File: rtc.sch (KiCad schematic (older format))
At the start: 8 parts, among them U3 RV-4162-C7

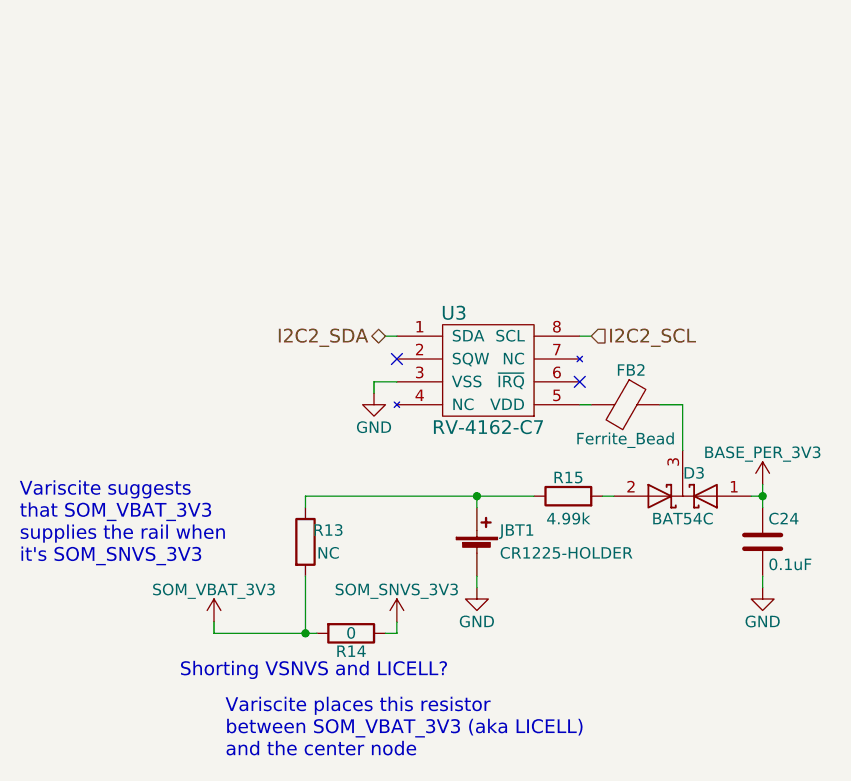
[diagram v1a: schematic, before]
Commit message: Add the board ID EEPROM chip and move the 0Ohm resistor such that the coin cell battery would actually power SOM_SNVS_3V3 when removed and the NC resistor is populated
This re-arrengment of the resistor makes the reference schematic more clear knowing that SOM_VBAT_3V3 is not actually LICELL.
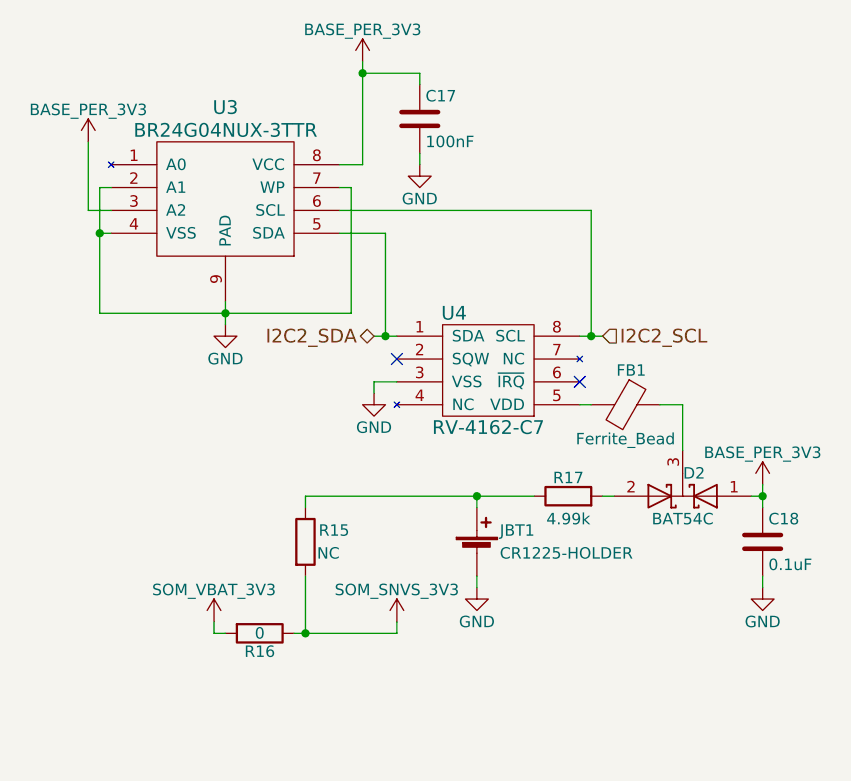
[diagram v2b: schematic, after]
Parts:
- added C17: 100nF, symbol C
- added U3: BR24G04NUX-3TTR, symbol BR24G04NUX-3TTR
- renumbered C24 to C18, D3 to D2, FB2 to FB1, R13 to R15, R14 to R16, R15 to R17, U3 to U4
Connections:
- net BASE_PER_3V3: now also C17.1, U3.3 (A2), U3.8 (VCC)
- net GND: now also C17.2, U3.2 (A1), U3.4 (VSS), U3.7 (WP), U3.9 (PAD)
- net I2C2_SCL: now also U3.6 (SCL)
- net I2C2_SDA: now also U3.5 (SDA)
- net SOM_SNVS_3V3: now also R15.2
- net SOM_VBAT_3V3: no longer R15.2
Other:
- note removed: "Shorting VSNVS and LICELL?"
- note removed: "Variscite places this resistor\nbetween SOM_VBAT_3V3 (aka LICELL)\nand the center node"
- note removed: "Variscite suggests\nthat SOM_VBAT_3V3\nsupplies the rail when\nit's SOM_SNVS_3V3"
- moved on the sheet: R16
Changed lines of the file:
@@
 $EndDescr
 $Comp
-L SOM_SNVS_3V3 #PWR041
+L SOM_SNVS_3V3 #PWR040
 U 1 1 5AC54E36
 P 5100 4300
-F 0 "#PWR041" H 5100 4150 50  0001 C CNN
+F 0 "#PWR040" H 5100 4150 50  0001 C CNN
 F 1 "SOM_SNVS_3V3" H 5100 4440 50  0000 C CNN
 F 2 "" H 5100 4300 50  0001 C CNN
@@
 $EndComp
 $Comp
-L R R14
+L R R16
 U 1 1 5AC54E4A
-P 4900 4350
-F 0 "R14" V 4980 4350 50  0000 C CNN
-F 1 "0" V 4900 4350 50  0000 C CNN
-F 2 "" V 4830 4350 50  0001 C CNN
-F 3 "" H 4900 4350 50  0001 C CNN
-	1    4900 4350
+P 4500 4350
+F 0 "R16" V 4580 4350 50  0000 C CNN
+F 1 "0" V 4500 4350 50  0000 C CNN
+F 2 "" V 4430 4350 50  0001 C CNN
+F 3 "" H 4500 4350 50  0001 C CNN
+	1    4500 4350
 	0    1    1    0
 $EndComp
 $Comp
-L SOM_VBAT_3V3 #PWR042
+L SOM_VBAT_3V3 #PWR041
 U 1 1 5AC54E9B
 P 4300 4300
-F 0 "#PWR042" H 4300 4150 50  0001 C CNN
+F 0 "#PWR041" H 4300 4150 50  0001 C CNN
 F 1 "SOM_VBAT_3V3" H 4300 4440 50  0000 C CNN
 F 2 "" H 4300 4300 50  0001 C CNN
@@
 	4300 4300 4300 4350
 $Comp
-L R R13
+L R R15
 U 1 1 5AC553FE
 P 4700 3950
-F 0 "R13" H 4800 4000 50  0000 C CNN
+F 0 "R15" H 4825 4000 50  0000 C CNN
 F 1 "NC" H 4800 3900 50  0000 C CNN
 F 2 "" V 4630 3950 50  0001 C CNN
@@
 $EndComp
 $Comp
-L D_Schottky_x2_KCom_AAK D3
+L D_Schottky_x2_KCom_AAK D2
 U 1 1 5AC55F7F
 P 6350 3750
-F 0 "D3" H 6300 3650 50  0000 C CNN
+F 0 "D2" H 6300 3650 50  0000 C CNN
 F 1 "BAT54C" H 6350 3850 50  0000 C CNN
 F 2 "" H 6350 3750 50  0001 C CNN
@@
 $EndComp
 $Comp
-L BASE_PER_3V3 #PWR043
+L BASE_PER_3V3 #PWR042
 U 1 1 5AC5AC58
 P 6700 3700
-F 0 "#PWR043" H 6700 3550 50  0001 C CNN
+F 0 "#PWR042" H 6700 3550 50  0001 C CNN
 F 1 "BASE_PER_3V3" H 6700 3840 50  0000 C CNN
 F 2 "" H 6700 3700 50  0001 C CNN
@@
 	6700 3700 6700 3800
 $Comp
-L R R15
+L R R17
 U 1 1 5AC5AF1B
 P 5850 3750
-F 0 "R15" V 5930 3750 50  0000 C CNN
+F 0 "R17" V 5930 3750 50  0000 C CNN
 F 1 "4.99k" V 5750 3750 50  0000 C CNN
 F 2 "" V 5780 3750 50  0001 C CNN
@@
 $EndComp
 $Comp
-L Ferrite_Bead FB2
+L Ferrite_Bead FB1
 U 1 1 5AC5AF7B
 P 6100 3350
-F 0 "FB2" V 5950 3375 50  0000 C CNN
+F 0 "FB1" V 5950 3375 50  0000 C CNN
 F 1 "Ferrite_Bead" V 6250 3350 50  0000 C CNN
 F 2 "" V 6030 3350 50  0001 C CNN
@@
 	6050 3750 6000 3750
 $Comp
-L C C24
+L C C18
 U 1 1 5AC5B61C
 P 6700 3950
-F 0 "C24" H 6725 4050 50  0000 L CNN
+F 0 "C18" H 6725 4050 50  0000 L CNN
 F 1 "0.1uF" H 6725 3850 50  0000 L CNN
 F 2 "" H 6738 3800 50  0001 C CNN
@@
 $EndComp
 $Comp
-L GND #PWR044
+L GND #PWR043
 U 1 1 5AC5B669
 P 6700 4150
-F 0 "#PWR044" H 6700 3900 50  0001 C CNN
+F 0 "#PWR043" H 6700 3900 50  0001 C CNN
 F 1 "GND" H 6700 4000 50  0000 C CNN
 F 2 "" H 6700 4150 50  0001 C CNN
@@
 Connection ~ 6700 3750
 $Comp
-L RV-4162-C7 U3
+L RV-4162-C7 U4
 U 1 1 5AC5BD52
 P 5500 3200
-F 0 "U3" H 5350 3450 60  0000 C CNN
+F 0 "U4" H 5350 3450 60  0000 C CNN
 F 1 "RV-4162-C7" H 5500 2950 60  0000 C CNN
 F 2 "" H 5600 2950 60  0001 C CNN
@@
 	4700 3750 5700 3750
 $Comp
-L GND #PWR045
+L GND #PWR044
 U 1 1 5AC5D6B6
 P 5450 4150
-F 0 "#PWR045" H 5450 3900 50  0001 C CNN
+F 0 "#PWR044" H 5450 3900 50  0001 C CNN
 F 1 "GND" H 5450 4000 50  0000 C CNN
 F 2 "" H 5450 4150 50  0001 C CNN
@@
 	4700 3800 4700 3750
 Connection ~ 5450 3750
-Text Notes 4350 4900 0    60   ~ 0
-Variscite places this resistor\nbetween SOM_VBAT_3V3 (aka LICELL)\nand the center node
-Text Notes 3450 4050 0    60   ~ 0
-Variscite suggests\nthat SOM_VBAT_3V3\nsupplies the rail when\nit's SOM_SNVS_3V3
-Wire Wire Line
-	5050 4350 5100 4350
-Wire Wire Line
-	4300 4350 4750 4350
-Text Notes 4150 4550 0    60   ~ 0
-Shorting VSNVS and LICELL?
-Text HLabel 5050 3050 0    60   BiDi ~ 0
+Text HLabel 5000 3050 0    60   BiDi ~ 0
 I2C2_SDA
-Text HLabel 5950 3050 2    60   Input ~ 0
+Text HLabel 6000 3050 2    60   Input ~ 0
 I2C2_SCL
 Wire Wire Line
-	5050 3050 5100 3050
-Wire Wire Line
-	5950 3050 5900 3050
-$Comp
-L GND #PWR046
+	5000 3050 5100 3050
+Wire Wire Line
+	5900 3050 6000 3050
+$Comp
+L GND #PWR045
 U 1 1 5AC6302E
 P 5000 3300
-F 0 "#PWR046" H 5000 3050 50  0001 C CNN
+F 0 "#PWR045" H 5000 3050 50  0001 C CNN
 F 1 "GND" H 5000 3150 50  0000 C CNN
 F 2 "" H 5000 3300 50  0001 C CNN
@@
 NoConn ~ 5900 3250
 NoConn ~ 5100 3150
+$Comp
+L BASE_PER_3V3 #PWR046
+U 1 1 5AC84D25
+P 3750 2200
+F 0 "#PWR046" H 3750 2050 50  0001 C CNN
+F 1 "BASE_PER_3V3" H 3750 2340 50  0000 C CNN
+F 2 "" H 3750 2200 50  0001 C CNN
+F 3 "" H 3750 2200 50  0001 C CNN
+	1    3750 2200
+	1    0    0    -1
+$EndComp
+$Comp
+L BASE_PER_3V3 #PWR047
+U 1 1 5AC84D64
+P 4950 1850
+F 0 "#PWR047" H 4950 1700 50  0001 C CNN
+F 1 "BASE_PER_3V3" H 4950 1990 50  0000 C CNN
+F 2 "" H 4950 1850 50  0001 C CNN
+F 3 "" H 4950 1850 50  0001 C CNN
+	1    4950 1850
+	1    0    0    -1
+$EndComp
+Wire Wire Line
+	3750 2200 3750 2500
+Wire Wire Line
+	3750 2500 3850 2500
+Wire Wire Line
+	4950 2300 4850 2300
+Wire Wire Line
+	4950 1850 4950 2300
+$Comp
+L BR24G04NUX-3TTR U3
+U 1 1 5AC850DC
+P 4350 2450
+F 0 "U3" H 4350 2850 60  0000 C CNN
+F 1 "BR24G04NUX-3TTR" H 4350 2750 60  0000 C CNN
+F 2 "" H 4350 2300 60  0001 C CNN
+F 3 "http://rohmfs.rohm.com/en/products/databook/datasheet/ic/memory/eeprom/br24g04-3-e.pdf" H 4350 2300 60  0001 C CNN
+F 4 "Rohm" H 4350 2450 60  0001 C CNN "MFG Name"
+F 5 "BR24G04NUX-3TTR" H 4350 2450 60  0001 C CNN "MFG Part Num"
+F 6 "BR24G04NUX-3TCT-ND" H 4350 2450 60  0001 C CNN "Distrib PN"
+F 7 "https://www.digikey.com/product-detail/en/rohm-semiconductor/BR24G04NUX-3TTR/BR24G04NUX-3TCT-ND/7807100" H 4350 2450 60  0001 C CNN "Distrib Link"
+F 8 "-" H 4350 2450 60  0001 C CNN "Tolerance"
+F 9 "https://www.digikey.com/products/en/integrated-circuits-ics/memory/774?FV=mu400kHz%7C800%2C142c1646%2C1f140000%2C1fec0002%2Cffe00306%2C23805c1%2C23805d8%2C238063b%2C2380664%2C238068b%2C23806a8&quantity=&ColumnSort=1000011&page=1&pageSize=500" H 4350 2450 60  0001 C CNN "Others"
+	1    4350 2450
+	1    0    0    -1
+$EndComp
+Wire Wire Line
+	3850 2400 3800 2400
+Wire Wire Line
+	3800 2400 3800 2950
+Wire Wire Line
+	3800 2950 4900 2950
+Wire Wire Line
+	4350 2900 4350 3000
+Wire Wire Line
+	4850 2400 4900 2400
+Wire Wire Line
+	4900 2400 4900 2950
+Connection ~ 4350 2950
+Wire Wire Line
+	3850 2600 3800 2600
+Connection ~ 3800 2600
+$Comp
+L GND #PWR048
+U 1 1 5AC8586C
+P 4350 3000
+F 0 "#PWR048" H 4350 2750 50  0001 C CNN
+F 1 "GND" H 4350 2850 50  0000 C CNN
+F 2 "" H 4350 3000 50  0001 C CNN
+F 3 "" H 4350 3000 50  0001 C CNN
+	1    4350 3000
+	1    0    0    -1
+$EndComp
+Wire Wire Line
+	4850 2600 5050 2600
+Wire Wire Line
+	5050 2600 5050 3050
+Connection ~ 5050 3050
+Wire Wire Line
+	4850 2500 5950 2500
+Wire Wire Line
+	5950 2500 5950 3050
+Connection ~ 5950 3050
+$Comp
+L C C17
+U 1 1 5AC8752C
+P 5200 2100
+F 0 "C17" H 5225 2200 50  0000 L CNN
+F 1 "100nF" H 5225 2000 50  0000 L CNN
+F 2 "" H 5238 1950 50  0001 C CNN
+F 3 "" H 5200 2100 50  0001 C CNN
+	1    5200 2100
+	1    0    0    -1
+$EndComp
+$Comp
+L GND #PWR049
+U 1 1 5AC875D7
+P 5200 2300
+F 0 "#PWR049" H 5200 2050 50  0001 C CNN
+F 1 "GND" H 5200 2150 50  0000 C CNN
+F 2 "" H 5200 2300 50  0001 C CNN
+F 3 "" H 5200 2300 50  0001 C CNN
+	1    5200 2300
+	1    0    0    -1
+$EndComp
+Wire Wire Line
+	5200 1950 5200 1900
+Wire Wire Line
+	5200 1900 4950 1900
+Connection ~ 4950 1900
+Wire Wire Line
+	5200 2300 5200 2250
+Wire Wire Line
+	4300 4350 4350 4350
+Wire Wire Line
+	4650 4350 5100 4350
 $EndSCHEMATC

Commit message: Add reset & watchdog, sd power, and BASE_PER_1V8 circuits
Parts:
- renumbered C17 to C20, C18 to C21, D2 to D3, R16 to R19, R15 to R20, R17 to R21, U3 to U4, U4 to U5
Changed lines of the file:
@@
 $Descr A4 11693 8268
 encoding utf-8
-Sheet 4 5
-Title ""
-Date ""
-Rev ""
-Comp ""
-Comment1 ""
-Comment2 ""
+Sheet 4 6
+Title "RTC Battery"
+Date "2018-04-05"
+Rev "v0.1.0"
+Comp "Purism SPC"
+Comment1 "Copyright 2018"
+Comment2 "GNU GPLv3"
 Comment3 ""
 Comment4 ""
 $EndDescr
 $Comp
-L SOM_SNVS_3V3 #PWR040
+L SOM_SNVS_3V3 #PWR048
 U 1 1 5AC54E36
 P 5100 4300
-F 0 "#PWR040" H 5100 4150 50  0001 C CNN
+F 0 "#PWR048" H 5100 4150 50  0001 C CNN
 F 1 "SOM_SNVS_3V3" H 5100 4440 50  0000 C CNN
 F 2 "" H 5100 4300 50  0001 C CNN
@@
 $EndComp
 $Comp
-L R R16
+L R R19
 U 1 1 5AC54E4A
 P 4500 4350
-F 0 "R16" V 4580 4350 50  0000 C CNN
+F 0 "R19" V 4580 4350 50  0000 C CNN
 F 1 "0" V 4500 4350 50  0000 C CNN
 F 2 "" V 4430 4350 50  0001 C CNN
@@
 $EndComp
 $Comp
-L SOM_VBAT_3V3 #PWR041
+L SOM_VBAT_3V3 #PWR049
 U 1 1 5AC54E9B
 P 4300 4300
-F 0 "#PWR041" H 4300 4150 50  0001 C CNN
+F 0 "#PWR049" H 4300 4150 50  0001 C CNN
 F 1 "SOM_VBAT_3V3" H 4300 4440 50  0000 C CNN
 F 2 "" H 4300 4300 50  0001 C CNN
@@
 	4300 4300 4300 4350
 $Comp
-L R R15
+L R R20
 U 1 1 5AC553FE
 P 4700 3950
-F 0 "R15" H 4825 4000 50  0000 C CNN
+F 0 "R20" H 4825 4000 50  0000 C CNN
 F 1 "NC" H 4800 3900 50  0000 C CNN
 F 2 "" V 4630 3950 50  0001 C CNN
@@
 $EndComp
 $Comp
-L D_Schottky_x2_KCom_AAK D2
+L D_Schottky_x2_KCom_AAK D3
 U 1 1 5AC55F7F
 P 6350 3750
-F 0 "D2" H 6300 3650 50  0000 C CNN
+F 0 "D3" H 6300 3650 50  0000 C CNN
 F 1 "BAT54C" H 6350 3850 50  0000 C CNN
 F 2 "" H 6350 3750 50  0001 C CNN
@@
 $EndComp
 $Comp
-L BASE_PER_3V3 #PWR042
+L BASE_PER_3V3 #PWR050
 U 1 1 5AC5AC58
 P 6700 3700
-F 0 "#PWR042" H 6700 3550 50  0001 C CNN
+F 0 "#PWR050" H 6700 3550 50  0001 C CNN
 F 1 "BASE_PER_3V3" H 6700 3840 50  0000 C CNN
 F 2 "" H 6700 3700 50  0001 C CNN
@@
 	6700 3700 6700 3800
 $Comp
-L R R17
+L R R21
 U 1 1 5AC5AF1B
 P 5850 3750
-F 0 "R17" V 5930 3750 50  0000 C CNN
+F 0 "R21" V 5930 3750 50  0000 C CNN
 F 1 "4.99k" V 5750 3750 50  0000 C CNN
 F 2 "" V 5780 3750 50  0001 C CNN
@@
 	6050 3750 6000 3750
 $Comp
-L C C18
+L C C21
 U 1 1 5AC5B61C
 P 6700 3950
-F 0 "C18" H 6725 4050 50  0000 L CNN
+F 0 "C21" H 6725 4050 50  0000 L CNN
 F 1 "0.1uF" H 6725 3850 50  0000 L CNN
 F 2 "" H 6738 3800 50  0001 C CNN
@@
 $EndComp
 $Comp
-L GND #PWR043
+L GND #PWR051
 U 1 1 5AC5B669
 P 6700 4150
-F 0 "#PWR043" H 6700 3900 50  0001 C CNN
+F 0 "#PWR051" H 6700 3900 50  0001 C CNN
 F 1 "GND" H 6700 4000 50  0000 C CNN
 F 2 "" H 6700 4150 50  0001 C CNN
@@
 Connection ~ 6700 3750
 $Comp
-L RV-4162-C7 U4
+L RV-4162-C7 U5
 U 1 1 5AC5BD52
 P 5500 3200
-F 0 "U4" H 5350 3450 60  0000 C CNN
+F 0 "U5" H 5350 3450 60  0000 C CNN
 F 1 "RV-4162-C7" H 5500 2950 60  0000 C CNN
 F 2 "" H 5600 2950 60  0001 C CNN
@@
 	4700 3750 5700 3750
 $Comp
-L GND #PWR044
+L GND #PWR052
 U 1 1 5AC5D6B6
 P 5450 4150
-F 0 "#PWR044" H 5450 3900 50  0001 C CNN
+F 0 "#PWR052" H 5450 3900 50  0001 C CNN
 F 1 "GND" H 5450 4000 50  0000 C CNN
 F 2 "" H 5450 4150 50  0001 C CNN
@@
 	5900 3050 6000 3050
 $Comp
-L GND #PWR045
+L GND #PWR053
 U 1 1 5AC6302E
 P 5000 3300
-F 0 "#PWR045" H 5000 3050 50  0001 C CNN
+F 0 "#PWR053" H 5000 3050 50  0001 C CNN
 F 1 "GND" H 5000 3150 50  0000 C CNN
 F 2 "" H 5000 3300 50  0001 C CNN
@@
 NoConn ~ 5100 3150
 $Comp
-L BASE_PER_3V3 #PWR046
+L BASE_PER_3V3 #PWR054
 U 1 1 5AC84D25
 P 3750 2200
-F 0 "#PWR046" H 3750 2050 50  0001 C CNN
+F 0 "#PWR054" H 3750 2050 50  0001 C CNN
 F 1 "BASE_PER_3V3" H 3750 2340 50  0000 C CNN
 F 2 "" H 3750 2200 50  0001 C CNN
@@
 $EndComp
 $Comp
-L BASE_PER_3V3 #PWR047
+L BASE_PER_3V3 #PWR055
 U 1 1 5AC84D64
 P 4950 1850
-F 0 "#PWR047" H 4950 1700 50  0001 C CNN
+F 0 "#PWR055" H 4950 1700 50  0001 C CNN
 F 1 "BASE_PER_3V3" H 4950 1990 50  0000 C CNN
 F 2 "" H 4950 1850 50  0001 C CNN
@@
 	4950 1850 4950 2300
 $Comp
-L BR24G04NUX-3TTR U3
+L BR24G04NUX-3TTR U4
 U 1 1 5AC850DC
 P 4350 2450
-F 0 "U3" H 4350 2850 60  0000 C CNN
+F 0 "U4" H 4350 2850 60  0000 C CNN
 F 1 "BR24G04NUX-3TTR" H 4350 2750 60  0000 C CNN
 F 2 "" H 4350 2300 60  0001 C CNN
@@
 Connection ~ 3800 2600
 $Comp
-L GND #PWR048
+L GND #PWR056
 U 1 1 5AC8586C
 P 4350 3000
-F 0 "#PWR048" H 4350 2750 50  0001 C CNN
+F 0 "#PWR056" H 4350 2750 50  0001 C CNN
 F 1 "GND" H 4350 2850 50  0000 C CNN
 F 2 "" H 4350 3000 50  0001 C CNN
@@
 Connection ~ 5950 3050
 $Comp
-L C C17
+L C C20
 U 1 1 5AC8752C
 P 5200 2100
-F 0 "C17" H 5225 2200 50  0000 L CNN
+F 0 "C20" H 5225 2200 50  0000 L CNN
 F 1 "100nF" H 5225 2000 50  0000 L CNN
 F 2 "" H 5238 1950 50  0001 C CNN
@@
 $EndComp
 $Comp
-L GND #PWR049
+L GND #PWR057
 U 1 1 5AC875D7
 P 5200 2300
-F 0 "#PWR049" H 5200 2050 50  0001 C CNN
+F 0 "#PWR057" H 5200 2050 50  0001 C CNN
 F 1 "GND" H 5200 2150 50  0000 C CNN
 F 2 "" H 5200 2300 50  0001 C CNN

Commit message: Add PTC Fuse, zener on VCC_PJ, USB PD current-limiting switch, 5V regulator, and make regulators' VINA=VIN (since VIH is 1.2V)
Equation for setting NX5P3090's current limit is included.
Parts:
- renumbered C20 to C22, C21 to C23, D3 to D4, R19 to R22, R20 to R23, R21 to R24, U4 to U5, U5 to U6
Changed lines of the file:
@@
 $Descr A4 11693 8268
 encoding utf-8
-Sheet 4 6
+Sheet 4 7
 Title "RTC Battery"
 Date "2018-04-05"
@@
 $EndDescr
 $Comp
-L SOM_SNVS_3V3 #PWR048
+L SOM_SNVS_3V3 #PWR055
 U 1 1 5AC54E36
 P 5100 4300
-F 0 "#PWR048" H 5100 4150 50  0001 C CNN
+F 0 "#PWR055" H 5100 4150 50  0001 C CNN
 F 1 "SOM_SNVS_3V3" H 5100 4440 50  0000 C CNN
 F 2 "" H 5100 4300 50  0001 C CNN
@@
 $EndComp
 $Comp
-L R R19
+L R R22
 U 1 1 5AC54E4A
 P 4500 4350
-F 0 "R19" V 4580 4350 50  0000 C CNN
+F 0 "R22" V 4580 4350 50  0000 C CNN
 F 1 "0" V 4500 4350 50  0000 C CNN
 F 2 "" V 4430 4350 50  0001 C CNN
@@
 $EndComp
 $Comp
-L SOM_VBAT_3V3 #PWR049
+L SOM_VBAT_3V3 #PWR056
 U 1 1 5AC54E9B
 P 4300 4300
-F 0 "#PWR049" H 4300 4150 50  0001 C CNN
+F 0 "#PWR056" H 4300 4150 50  0001 C CNN
 F 1 "SOM_VBAT_3V3" H 4300 4440 50  0000 C CNN
 F 2 "" H 4300 4300 50  0001 C CNN
@@
 	4300 4300 4300 4350
 $Comp
-L R R20
+L R R23
 U 1 1 5AC553FE
 P 4700 3950
-F 0 "R20" H 4825 4000 50  0000 C CNN
+F 0 "R23" H 4825 4000 50  0000 C CNN
 F 1 "NC" H 4800 3900 50  0000 C CNN
 F 2 "" V 4630 3950 50  0001 C CNN
@@
 $EndComp
 $Comp
-L D_Schottky_x2_KCom_AAK D3
+L D_Schottky_x2_KCom_AAK D4
 U 1 1 5AC55F7F
 P 6350 3750
-F 0 "D3" H 6300 3650 50  0000 C CNN
+F 0 "D4" H 6300 3650 50  0000 C CNN
 F 1 "BAT54C" H 6350 3850 50  0000 C CNN
 F 2 "" H 6350 3750 50  0001 C CNN
@@
 $EndComp
 $Comp
-L BASE_PER_3V3 #PWR050
+L BASE_PER_3V3 #PWR057
 U 1 1 5AC5AC58
 P 6700 3700
-F 0 "#PWR050" H 6700 3550 50  0001 C CNN
+F 0 "#PWR057" H 6700 3550 50  0001 C CNN
 F 1 "BASE_PER_3V3" H 6700 3840 50  0000 C CNN
 F 2 "" H 6700 3700 50  0001 C CNN
@@
 	6700 3700 6700 3800
 $Comp
-L R R21
+L R R24
 U 1 1 5AC5AF1B
 P 5850 3750
-F 0 "R21" V 5930 3750 50  0000 C CNN
+F 0 "R24" V 5930 3750 50  0000 C CNN
 F 1 "4.99k" V 5750 3750 50  0000 C CNN
 F 2 "" V 5780 3750 50  0001 C CNN
@@
 	6050 3750 6000 3750
 $Comp
-L C C21
+L C C23
 U 1 1 5AC5B61C
 P 6700 3950
-F 0 "C21" H 6725 4050 50  0000 L CNN
+F 0 "C23" H 6725 4050 50  0000 L CNN
 F 1 "0.1uF" H 6725 3850 50  0000 L CNN
 F 2 "" H 6738 3800 50  0001 C CNN
@@
 $EndComp
 $Comp
-L GND #PWR051
+L GND #PWR058
 U 1 1 5AC5B669
 P 6700 4150
-F 0 "#PWR051" H 6700 3900 50  0001 C CNN
+F 0 "#PWR058" H 6700 3900 50  0001 C CNN
 F 1 "GND" H 6700 4000 50  0000 C CNN
 F 2 "" H 6700 4150 50  0001 C CNN
@@
 Connection ~ 6700 3750
 $Comp
-L RV-4162-C7 U5
+L RV-4162-C7 U6
 U 1 1 5AC5BD52
 P 5500 3200
-F 0 "U5" H 5350 3450 60  0000 C CNN
+F 0 "U6" H 5350 3450 60  0000 C CNN
 F 1 "RV-4162-C7" H 5500 2950 60  0000 C CNN
 F 2 "" H 5600 2950 60  0001 C CNN
@@
 	4700 3750 5700 3750
 $Comp
-L GND #PWR052
+L GND #PWR059
 U 1 1 5AC5D6B6
 P 5450 4150
-F 0 "#PWR052" H 5450 3900 50  0001 C CNN
+F 0 "#PWR059" H 5450 3900 50  0001 C CNN
 F 1 "GND" H 5450 4000 50  0000 C CNN
 F 2 "" H 5450 4150 50  0001 C CNN
@@
 	5900 3050 6000 3050
 $Comp
-L GND #PWR053
+L GND #PWR060
 U 1 1 5AC6302E
 P 5000 3300
-F 0 "#PWR053" H 5000 3050 50  0001 C CNN
+F 0 "#PWR060" H 5000 3050 50  0001 C CNN
 F 1 "GND" H 5000 3150 50  0000 C CNN
 F 2 "" H 5000 3300 50  0001 C CNN
@@
 NoConn ~ 5100 3150
 $Comp
-L BASE_PER_3V3 #PWR054
+L BASE_PER_3V3 #PWR061
 U 1 1 5AC84D25
 P 3750 2200
-F 0 "#PWR054" H 3750 2050 50  0001 C CNN
+F 0 "#PWR061" H 3750 2050 50  0001 C CNN
 F 1 "BASE_PER_3V3" H 3750 2340 50  0000 C CNN
 F 2 "" H 3750 2200 50  0001 C CNN
@@
 $EndComp
 $Comp
-L BASE_PER_3V3 #PWR055
+L BASE_PER_3V3 #PWR062
 U 1 1 5AC84D64
 P 4950 1850
-F 0 "#PWR055" H 4950 1700 50  0001 C CNN
+F 0 "#PWR062" H 4950 1700 50  0001 C CNN
 F 1 "BASE_PER_3V3" H 4950 1990 50  0000 C CNN
 F 2 "" H 4950 1850 50  0001 C CNN
@@
 	4950 1850 4950 2300
 $Comp
-L BR24G04NUX-3TTR U4
+L BR24G04NUX-3TTR U5
 U 1 1 5AC850DC
 P 4350 2450
-F 0 "U4" H 4350 2850 60  0000 C CNN
+F 0 "U5" H 4350 2850 60  0000 C CNN
 F 1 "BR24G04NUX-3TTR" H 4350 2750 60  0000 C CNN
 F 2 "" H 4350 2300 60  0001 C CNN
@@
 Connection ~ 3800 2600
 $Comp
-L GND #PWR056
+L GND #PWR063
 U 1 1 5AC8586C
 P 4350 3000
-F 0 "#PWR056" H 4350 2750 50  0001 C CNN
+F 0 "#PWR063" H 4350 2750 50  0001 C CNN
 F 1 "GND" H 4350 2850 50  0000 C CNN
 F 2 "" H 4350 3000 50  0001 C CNN
@@
 Connection ~ 5950 3050
 $Comp
-L C C20
+L C C22
 U 1 1 5AC8752C
 P 5200 2100
-F 0 "C20" H 5225 2200 50  0000 L CNN
+F 0 "C22" H 5225 2200 50  0000 L CNN
 F 1 "100nF" H 5225 2000 50  0000 L CNN
 F 2 "" H 5238 1950 50  0001 C CNN
@@
 $EndComp
 $Comp
-L GND #PWR057
+L GND #PWR064
 U 1 1 5AC875D7
 P 5200 2300
-F 0 "#PWR057" H 5200 2050 50  0001 C CNN
+F 0 "#PWR064" H 5200 2050 50  0001 C CNN
 F 1 "GND" H 5200 2150 50  0000 C CNN
 F 2 "" H 5200 2300 50  0001 C CNN
